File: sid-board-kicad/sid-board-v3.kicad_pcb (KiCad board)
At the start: 2 copper layers, 60.1 x 60.1 mm, 49 parts, among them J1 SPI, J2 UART, J3 Conn_01x08, Q1 BSS138, SW1 EN, SW2 FLASH, U1 SC16IS752, U2 MCP1703A-3302, U3 SN65HVD232 x3, U4 SN65HVD232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

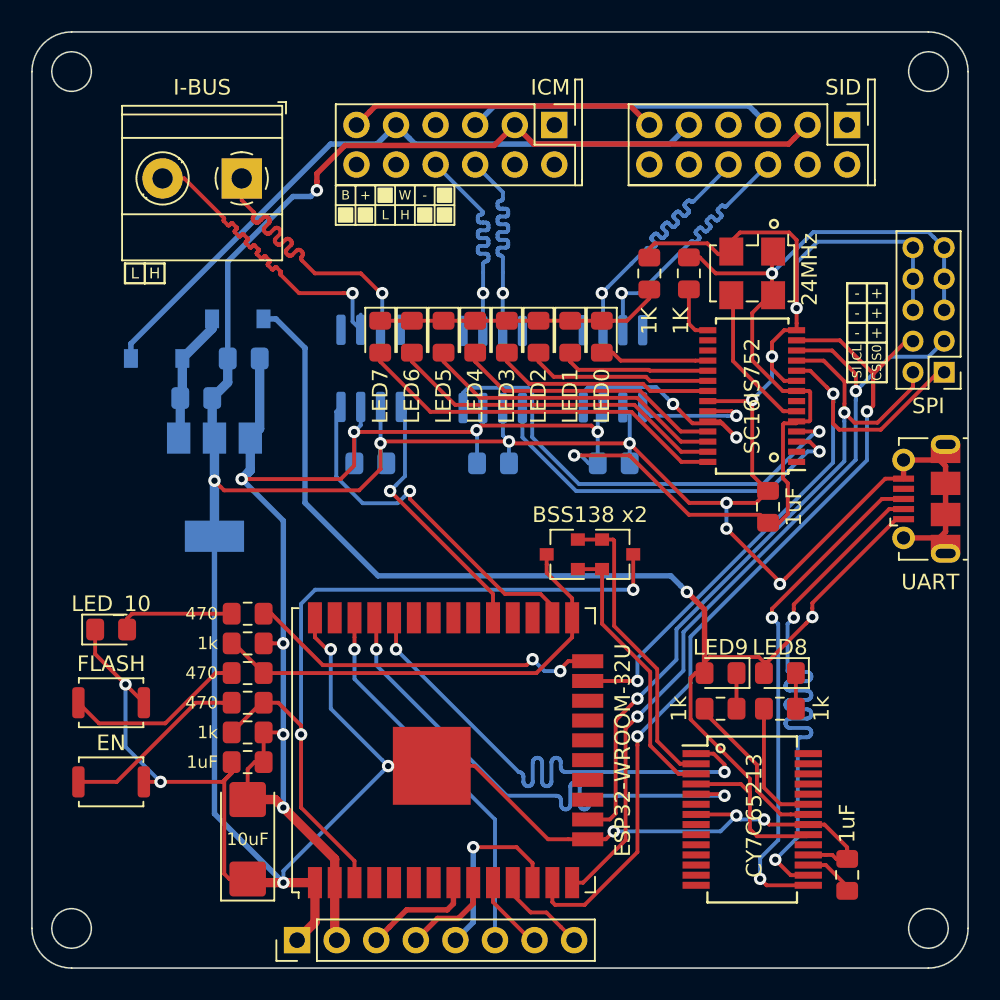
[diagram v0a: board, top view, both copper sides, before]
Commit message: Checked bootstrapping pins. Checked RX TX pins.
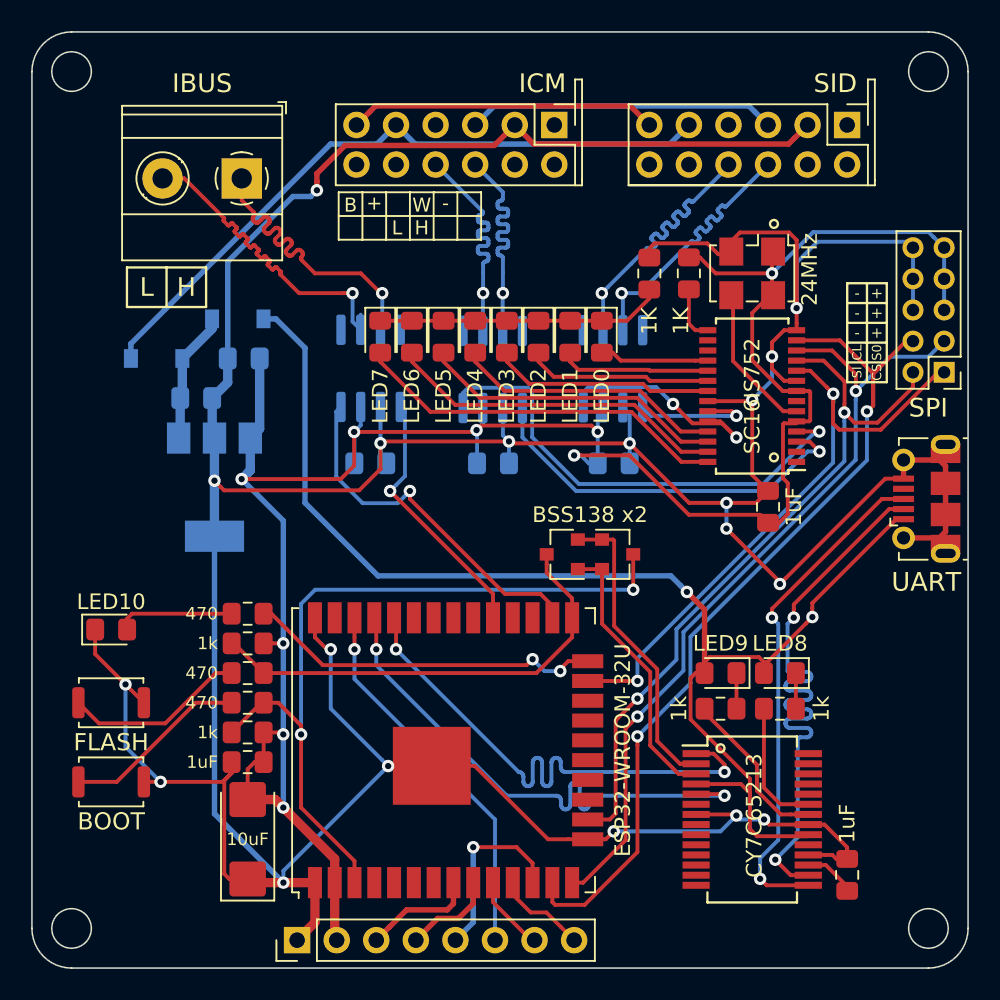
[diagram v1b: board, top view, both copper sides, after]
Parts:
- D9: value LED_10 -> LED10
- SW1: value EN -> BOOT
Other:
- board text added: "IBUS"
- board text removed: "I-BUS"

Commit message: Labelling.
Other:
- board text added: "LEIGH OLIVER 2020"
- board text added: "SAAB HPD INTERFACE v3"
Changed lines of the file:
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@@
   (general
     (thickness 1.6)
-    (drawings 82)
+    (drawings 84)
     (tracks 1757)
     (zones 0)
@@
   (layers
     (0 F.Cu signal)
-    (31 B.Cu signal)
-    (32 B.Adhes user)
-    (33 F.Adhes user)
-    (34 B.Paste user)
+    (31 B.Cu signal hide)
+    (32 B.Adhes user hide)
+    (33 F.Adhes user hide)
+    (34 B.Paste user hide)
     (35 F.Paste user)
-    (36 B.SilkS user)
+    (36 B.SilkS user hide)
     (37 F.SilkS user)
-    (38 B.Mask user)
+    (38 B.Mask user hide)
     (39 F.Mask user)
-    (40 Dwgs.User user)
-    (41 Cmts.User user)
-    (42 Eco1.User user)
-    (43 Eco2.User user)
+    (40 Dwgs.User user hide)
+    (41 Cmts.User user hide)
+    (42 Eco1.User user hide)
+    (43 Eco2.User user hide)
     (44 Edge.Cuts user)
-    (45 Margin user)
-    (46 B.CrtYd user)
+    (45 Margin user hide)
+    (46 B.CrtYd user hide)
     (47 F.CrtYd user)
-    (48 B.Fab user)
+    (48 B.Fab user hide)
     (49 F.Fab user)
   )
@@
       (effects (font (size 1 1) (thickness 0.15)))
     )
-    (fp_text value SPI (at 1.016 -2.286 180) (layer F.SilkS)
+    (fp_text value SPI (at 1.016 -2.54 180) (layer F.SilkS)
       (effects (font (size 1.2 1.2) (thickness 0.3)))
     )
@@
       (effects (font (size 1 1) (thickness 0.15)))
     )
-    (fp_text value UART (at -5.334 0 180) (layer F.SilkS)
+    (fp_text value UART (at -5.588 0 180) (layer F.SilkS)
       (effects (font (size 1.2 1.2) (thickness 0.3)))
     )
@@
     )
   )
+  (gr_text "LEIGH OLIVER 2020" (at 118.11 95.25) (layer F.SilkS)
+    (effects (font (size 1 1) (thickness 0.25)) (justify left))
+  )
+  (gr_text "SAAB HPD\nINTERFACE v3" (at 118.11 91.44) (layer F.SilkS)
+    (effects (font (size 1.5 1.5) (thickness 0.375)) (justify left))
+  )
   (gr_text H (at 122.682 79.629) (layer F.SilkS)
